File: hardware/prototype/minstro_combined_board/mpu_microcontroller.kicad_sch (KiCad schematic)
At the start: 50 parts, among them J301 BOOT, J302 UART, J303 USB_C_Receptacle_USB2.0_16P, J304 SDMMC 4b, J305 Conn_Coaxial, SW301 RST, U301 ESP32-S3, U302 W25Q128JVS, Y301 40 MHz

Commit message: Combined board started layout
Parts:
- renumbered AE301 to AE401, C301 to C401, C302 to C402, C303 to C403, C304 to C404, C305 to C405, C306 to C406, C307 to C407, C308 to C408, C309 to C409, C310 to C410, C311 to C411, C312 to C412, C313 to C413, C314 to C414, C315 to C415, D301 to D401, FB301 to FB401, J301 to J401, J302 to J402, J303 to J403, J304 to J404, J305 to J405, JP301 to JP401, L301 to L401, R301 to R401, R302 to R402, R303 to R403, R304 to R404, R305 to R405, R306 to R406, R307 to R407, R308 to R408, R309 to R409, R310 to R410, R311 to R411, R312 to R412, R313 to R413, R314 to R414, R315 to R415, R316 to R416, R317 to R417, R318 to R418, R319 to R419, R320 to R420, SW301 to SW401, U301 to U401, U302 to U402, U303 to U403, Y301 to Y401

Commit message: Schematic ERC complete
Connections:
- net SD_CS is gone; now on net SD_DET: U401.52 (GPIO46)
- net GND: now also J404.11 (SHIELD)
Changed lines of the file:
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@@
 	(wire
 		(pts
+			(xy 269.24 151.13) (xy 269.24 154.94)
+		)
+		(stroke
+			(width 0)
+			(type default)
+		)
+	)
+	(wire
+		(pts
 			(xy 166.37 110.49) (xy 166.37 106.68)
 		)
@@
 	(wire
 		(pts
+			(xy 269.24 154.94) (xy 271.78 154.94)
+		)
+		(stroke
+			(width 0)
+			(type default)
+		)
+	)
+	(wire
+		(pts
 			(xy 208.28 140.97) (xy 210.82 140.97)
 		)
@@
 	(wire
 		(pts
+			(xy 200.66 160.02) (xy 204.47 160.02)
+		)
+		(stroke
+			(width 0)
+			(type default)
+		)
+	)
+	(wire
+		(pts
 			(xy 107.95 104.14) (xy 114.3 104.14)
 		)
@@
 		)
 	)
-	(label "SD_CS"
-		(at 114.3 127 0)
-		(effects
-			(font
-				(size 1.27 1.27)
-			)
-			(justify left bottom)
-		)
-	)
 	(label "STATUS_LED"
 		(at 266.7 26.67 0)
@@
 		)
 	)
+	(label "SD_DET"
+		(at 114.3 127 0)
+		(effects
+			(font
+				(size 1.27 1.27)
+			)
+			(justify left bottom)
+		)
+	)
 	(label "VDD33"
 		(at 90.17 59.69 90)
@@
 		)
 	)
+	(hierarchical_label "V_usb"
+		(shape input)
+		(at 271.78 154.94 0)
+		(effects
+			(font
+				(size 1.27 1.27)
+			)
+			(justify left)
+		)
+	)
 	(hierarchical_label "DISP_TS_RST"
 		(shape input)
@@
 		(on_board yes)
 		(dnp no)
-		(property "Reference" "#PWR0421"
+		(property "Reference" "#PWR0422"
 			(at 69.85 175.26 0)
 			(effects
@@
 			(project "display_board"
 				(path "/edc2d64f-9cdb-4ab0-b2de-c3cfa55e1c10/f8b73dba-3bd2-4715-a78c-fbce9d68ac6b"
-					(reference "#PWR0421")
+					(reference "#PWR0422")
 					(unit 1)
 				)
@@
 	)
 	(symbol
+		(lib_id "power:GND")
+		(at 204.47 160.02 0)
+		(unit 1)
+		(exclude_from_sim no)
+		(in_bom yes)
+		(on_board yes)
+		(dnp no)
+		(fields_autoplaced yes)
+		(property "Reference" "#PWR0420"
+			(at 204.47 166.37 0)
+			(effects
+				(font
+					(size 1.27 1.27)
+				)
+				(hide yes)
+			)
+		)
+		(property "Value" "GND"
+			(at 204.47 165.1 0)
+			(effects
+				(font
+					(size 1.27 1.27)
+				)
+			)
+		)
+		(property "Footprint" ""
+			(at 204.47 160.02 0)
+			(effects
+				(font
+					(size 1.27 1.27)
+				)
+				(hide yes)
+			)
+		)
+		(property "Datasheet" ""
+			(at 204.47 160.02 0)
+			(effects
+				(font
+					(size 1.27 1.27)
+				)
+				(hide yes)
+			)
+		)
+		(property "Description" ""
+			(at 204.47 160.02 0)
+			(effects
+				(font
+					(size 1.27 1.27)
+				)
+				(hide yes)
+			)
+		)
+		(pin "1"
+		)
+		(instances
+			(project "minstro_combined_board"
+				(path "/edc2d64f-9cdb-4ab0-b2de-c3cfa55e1c10/f8b73dba-3bd2-4715-a78c-fbce9d68ac6b"
+					(reference "#PWR0420")
+					(unit 1)
+				)
+			)
+		)
+	)
+	(symbol
 		(lib_id "Device:FerriteBead_Small")
 		(at 68.58 36.83 90)
@@
 		(dnp no)
 		(fields_autoplaced yes)
-		(property "Reference" "#PWR0424"
+		(property "Reference" "#PWR0425"
 			(at 66.04 196.85 0)
 			(effects
@@
 			(project "display_board"
 				(path "/edc2d64f-9cdb-4ab0-b2de-c3cfa55e1c10/f8b73dba-3bd2-4715-a78c-fbce9d68ac6b"
-					(reference "#PWR0424")
+					(reference "#PWR0425")
 					(unit 1)
 				)
@@
 		(dnp no)
 		(fields_autoplaced yes)
-		(property "Reference" "#PWR0425"
+		(property "Reference" "#PWR0426"
 			(at 114.3 196.85 0)
 			(effects
@@
 			(project "display_board"
 				(path "/edc2d64f-9cdb-4ab0-b2de-c3cfa55e1c10/f8b73dba-3bd2-4715-a78c-fbce9d68ac6b"
-					(reference "#PWR0425")
+					(reference "#PWR0426")
+					(unit 1)
+				)
+			)
+		)
+	)
+	(symbol
+		(lib_id "power:PWR_FLAG")
+		(at 269.24 151.13 0)
+		(unit 1)
+		(exclude_from_sim no)
+		(in_bom yes)
+		(on_board yes)
+		(dnp no)
+		(fields_autoplaced yes)
+		(property "Reference" "#FLG0403"
+			(at 269.24 149.225 0)
+			(effects
+				(font
+					(size 1.27 1.27)
+				)
+				(hide yes)
+			)
+		)
+		(property "Value" "PWR_FLAG"
+			(at 269.24 146.05 0)
+			(effects
+				(font
+					(size 1.27 1.27)
+				)
+			)
+		)
+		(property "Footprint" ""
+			(at 269.24 151.13 0)
+			(effects
+				(font
+					(size 1.27 1.27)
+				)
+				(hide yes)
+			)
+		)
+		(property "Datasheet" "~"
+			(at 269.24 151.13 0)
+			(effects
+				(font
+					(size 1.27 1.27)
+				)
+				(hide yes)
+			)
+		)
+		(property "Description" "Special symbol for telling ERC where power comes from"
+			(at 269.24 151.13 0)
+			(effects
+				(font
+					(size 1.27 1.27)
+				)
+				(hide yes)
+			)
+		)
+		(pin "1"
+		)
+		(instances
+			(project ""
+				(path "/edc2d64f-9cdb-4ab0-b2de-c3cfa55e1c10/f8b73dba-3bd2-4715-a78c-fbce9d68ac6b"
+					(reference "#FLG0403")
 					(unit 1)
 				)
@@
 		(dnp no)
 		(fields_autoplaced yes)
-		(property "Reference" "#PWR0423"
+		(property "Reference" "#PWR0424"
 			(at 52.07 193.04 0)
 			(effects
@@
 			(project "display_board"
 				(path "/edc2d64f-9cdb-4ab0-b2de-c3cfa55e1c10/f8b73dba-3bd2-4715-a78c-fbce9d68ac6b"
-					(reference "#PWR0423")
+					(reference "#PWR0424")
 					(unit 1)
 				)
@@
 		(dnp no)
 		(fields_autoplaced yes)
-		(property "Reference" "#PWR0420"
+		(property "Reference" "#PWR0421"
 			(at 116.84 171.45 0)
 			(effects
@@
 			(project "display_board"
 				(path "/edc2d64f-9cdb-4ab0-b2de-c3cfa55e1c10/f8b73dba-3bd2-4715-a78c-fbce9d68ac6b"
-					(reference "#PWR0420")
+					(reference "#PWR0421")
 					(unit 1)
 				)
@@
 		(dnp no)
 		(fields_autoplaced yes)
-		(property "Reference" "#PWR0422"
+		(property "Reference" "#PWR0423"
 			(at 31.75 193.04 0)
 			(effects
@@
 			(project "display_board"
 				(path "/edc2d64f-9cdb-4ab0-b2de-c3cfa55e1c10/f8b73dba-3bd2-4715-a78c-fbce9d68ac6b"
-					(reference "#PWR0422")
+					(reference "#PWR0423")
 					(unit 1)
 				)

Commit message: Layout WIP
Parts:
- AE401: value Antenna_Shield -> ANT; footprint RF_Antenna:Texas_SWRA117D_2.4GHz_Right -> BVH_RF_Ham:ANT2012LL13R2400A
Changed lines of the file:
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@@
 		(on_board yes)
 		(dnp no)
-		(fields_autoplaced yes)
 		(property "Reference" "FB401"
-			(at 68.5419 30.48 90)
+			(at 68.58 33.528 90)
 			(effects
 				(font
@@
 			)
 		)
-		(property "Value" "Antenna_Shield"
+		(property "Value" "ANT"
 			(at 60.96 164.4649 0)
 			(effects
@@
 			)
 		)
-		(property "Footprint" "RF_Antenna:Texas_SWRA117D_2.4GHz_Right"
+		(property "Footprint" "BVH_RF_Ham:ANT2012LL13R2400A"
 			(at 57.15 161.29 0)
 			(effects

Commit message: Layout and routing Power and initial signals, SD card
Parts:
- removed J402: UART, Connector_PinHeader_2.54mm:PinHeader_1x03_P2.54mm_Vertical, symbol Connector_Generic:Conn_01x03
- removed R405: 499, Resistor_SMD:R_0603_1608Metric, symbol Device:R_Small
- U401: footprint Package_DFN_QFN:QFN-56-1EP_7x7mm_P0.4mm_EP4x4mm -> Package_DFN_QFN:QFN-56-1EP_7x7mm_P0.4mm_EP4x4mm_ThermalVias
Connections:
- net UART_RX is gone; now on net SD_DET: U401.50 (GPIO44/U0RXD)
- net UART_TX is gone; now on net SD_DAT2: U401.49 (GPIO43/U0TXD)
- net DISP_BL: now also U401.38 (GPIO33); no longer U401.27 (GPIO21)
- net DISP_CS: now also U401.27 (GPIO21); no longer U401.14 (GPIO9)
- net DISP_DC: now also U401.18 (GPIO13); no longer U401.13 (GPIO8)
- net DISP_RST: now also U401.24 (GPIO18); no longer U401.17 (GPIO12)
- net DISP_SCL: now also U401.19 (GPIO14); no longer U401.15 (GPIO10)
- net DISP_SDA: now also U401.23 (GPIO17); no longer U401.16 (GPIO11)
- net DISP_TS_INT: now also U401.21 (GPIO15/XTAL_32K_P*); no longer U401.18 (GPIO13)
- net DISP_TS_RST: now also U401.22 (GPIO16/XTAL_32K_N*); no longer U401.19 (GPIO14)
- net I2S_ADCIN: now also U401.14 (GPIO9); no longer U401.41 (GPIO36)
- net I2S_ADCOUT: now also U401.15 (GPIO10); no longer U401.40 (GPIO35)
- net I2S_BCLK: now also U401.16 (GPIO11); no longer U401.39 (GPIO34)
- net I2S_FS: now also U401.17 (GPIO12); no longer U401.38 (GPIO33)
- net I2S_MCLK: now also U401.13 (GPIO8); no longer U401.42 (GPIO37)
- net PWR_CHRG: now also U401.41 (GPIO36); no longer U401.21 (GPIO15/XTAL_32K_P*)
- net PWR_EXT: now also U401.42 (GPIO37); no longer U401.22 (GPIO16/XTAL_32K_N*)
- net SD_CMD: now also U401.47 (GPIO41/MTDI); no longer U401.51 (GPIO45)
- net SD_DAT1: now also U401.43 (GPIO38); no longer U401.45 (GPIO40/MTDO)
- net SD_DAT2: no longer U401.47 (GPIO41/MTDI)
- net SD_DET: no longer U401.24 (GPIO18), U401.52 (GPIO46)
- net SD_SCK: now also U401.45 (GPIO40/MTDO); no longer U401.43 (GPIO38)
- no-connect marks 9 -> 8
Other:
- note removed: "Resistor on TX line for harmonic suppression"
- moved on the sheet: C410

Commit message: Routing mostly completed
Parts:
- removed R403: 100k, Resistor_SMD:R_0603_1608Metric, symbol Device:R_Small
- J403: footprint Connector_USB:USB_C_Receptacle_GCT_USB4085 -> BVH_Connectors_Misc:USB_C_Receptacle_GCT_USB4085_PinPaste
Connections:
- net HMI_INT: now also U401.42 (GPIO37); no longer U401.8 (GPIO3)
- net HMI_WAKE: now also U401.41 (GPIO36); no longer U401.7 (GPIO2)
- net PWR_CHRG: now also U401.39 (GPIO34); no longer U401.41 (GPIO36)
- net PWR_EXT: now also U401.40 (GPIO35); no longer U401.42 (GPIO37)
- net USB_N: now also U403.1 (CH1); no longer U403.5 (CH4)
- net USB_P: now also U403.5 (CH4); no longer U403.4 (CH3)
- net MODE_SEL: no longer names the net of U401.6 (GPIO1)
- no-connect marks 8 -> 10
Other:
- note removed: "Resistor divider for mode selection Use with internal PU resistor Internal PU / PD Resistors are ~45k Ohm"

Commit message: Layout completed, initial review
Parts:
- added J402: I2C, BVH_PinHeader_FrictionRetention:PinHeader_1x04_P2.54mm_Vertical, symbol Connector_Generic:Conn_01x04
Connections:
- net +3.3V: now also J402.2 (Pin_2)
- net GND: now also J402.1 (Pin_1)
- net I2C_SCK: now also J402.4 (Pin_4)
- net I2C_SDA: now also J402.3 (Pin_3)

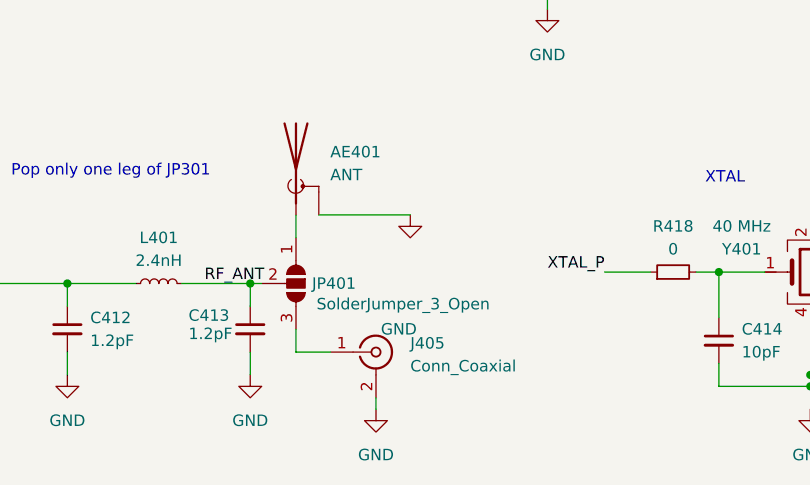
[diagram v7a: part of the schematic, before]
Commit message: Move slot and begin re-layout
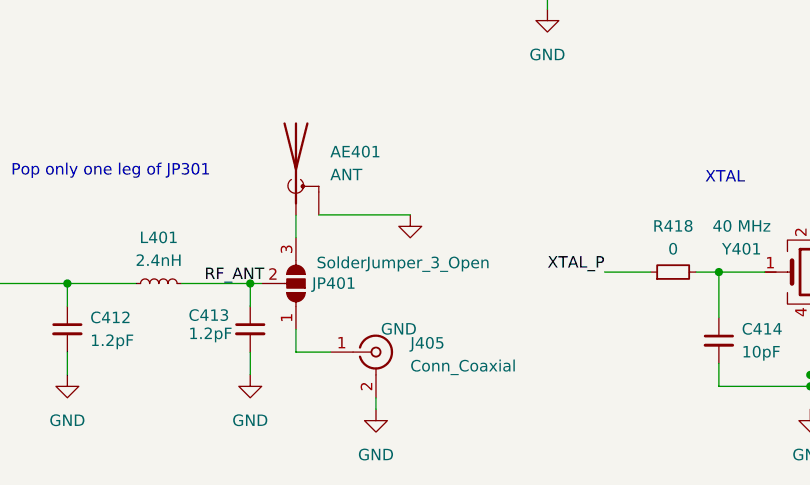
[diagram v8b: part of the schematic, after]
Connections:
- net at J405.1 (In): now also JP401.1 (A); no longer JP401.3 (B)
- net at AE401.1 (A): now also JP401.3 (B); no longer JP401.1 (A)
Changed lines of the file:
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@@
 		(lib_id "Jumper:SolderJumper_3_Open")
 		(at 57.15 176.53 270)
+		(mirror x)
 		(unit 1)
 		(exclude_from_sim yes)
@@
 		)
 		(property "Value" "SolderJumper_3_Open"
-			(at 59.436 178.816 90)
+			(at 59.436 174.244 90)
 			(effects
 				(font
